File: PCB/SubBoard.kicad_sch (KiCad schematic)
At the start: 37 parts, among them IC1 AS5047P-ATSM, IC2 AS5047P-ATSM, IC3 ICM-20648, J10 Conn_A_Sub, J11 Conn_MCU_L, J4 Conn_ENC_L, J5 SWD, J6 UART, J7 Conn_ENC_R, J8 Conn_MCU_R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

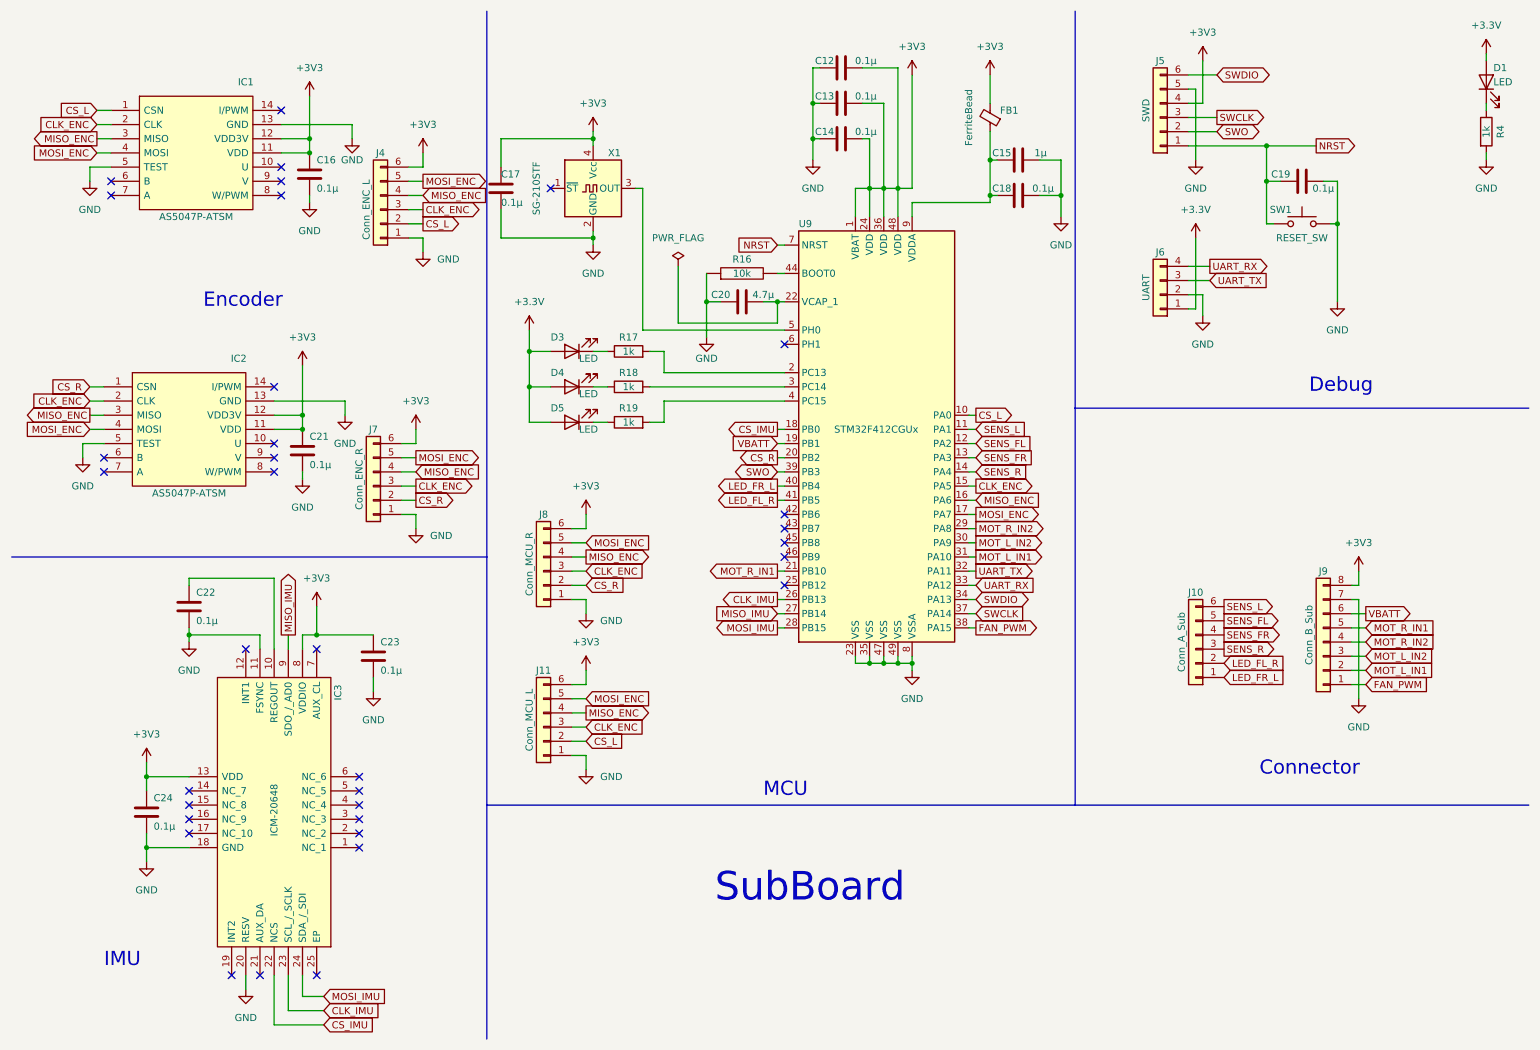
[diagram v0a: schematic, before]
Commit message: [fix]壁センサの配線ミスを修正
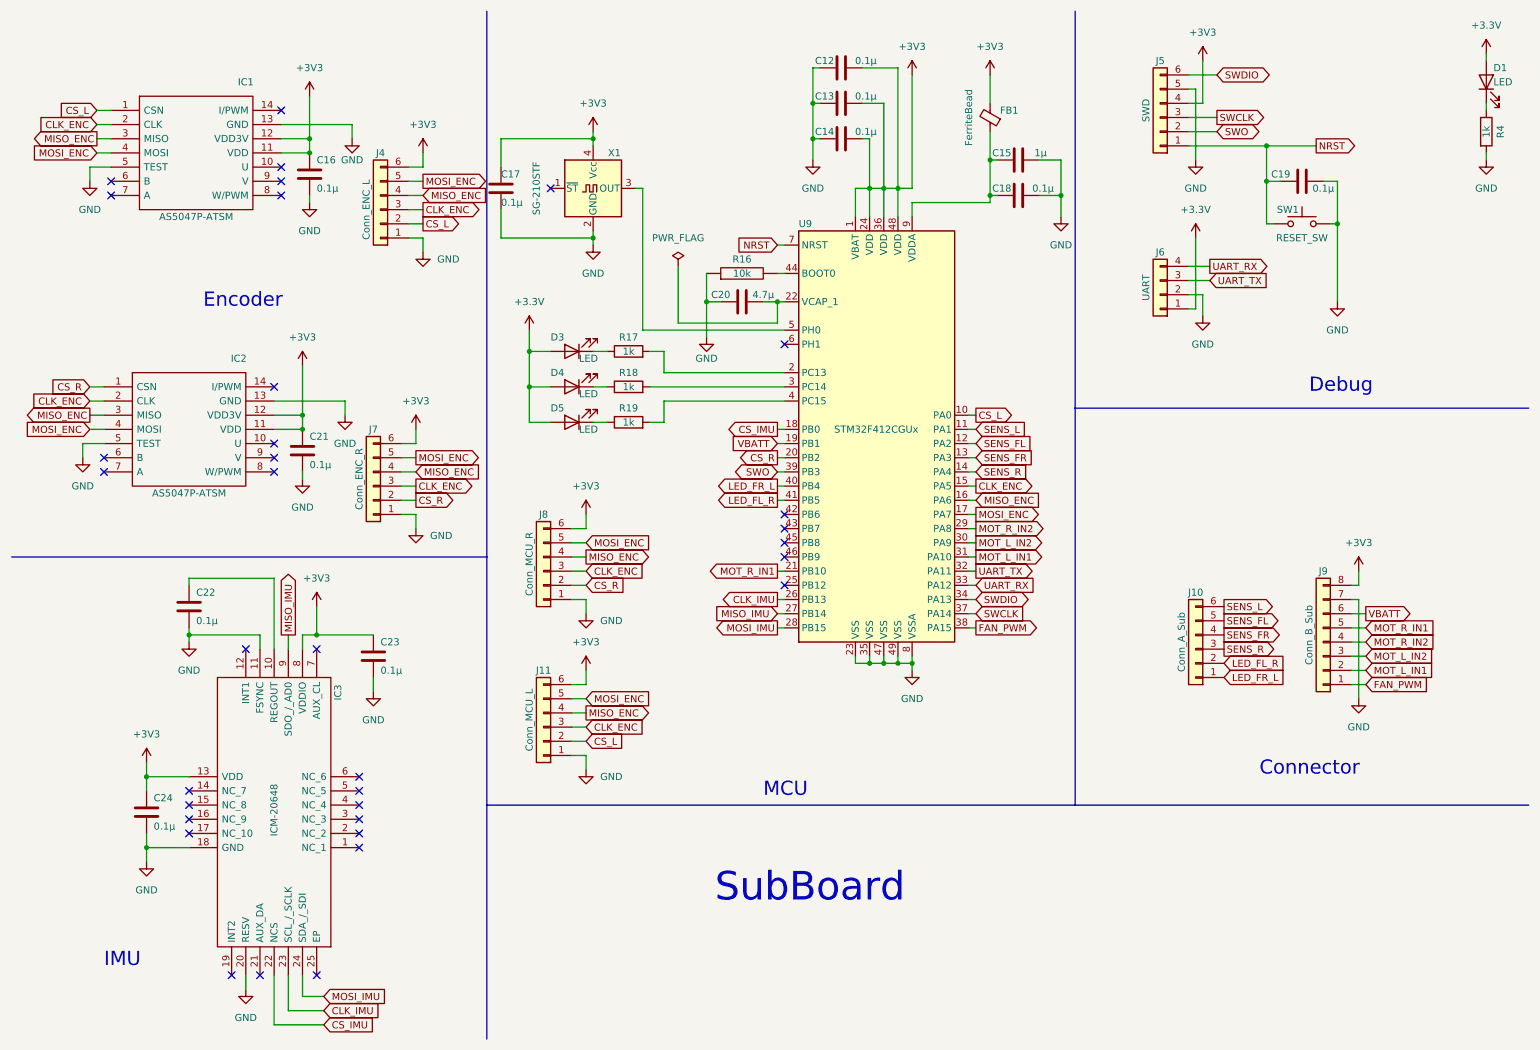
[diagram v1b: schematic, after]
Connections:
- net GND: no longer SW1.2 (A)
- net NRST: now also SW1.2; no longer SW1.3 (B), SW1.4 (B)
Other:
- moved on the sheet: SW1
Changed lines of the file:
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@@
     (pin "4")
   )
-  (symbol (lib_id "Switch:SW_Push") (at 247.65 50.8 270) (mirror x) (unit 1)
+  (symbol (lib_id "Switch:SW_Push") (at 243.84 50.8 0) (mirror y) (unit 1)
     (in_bom yes) (on_board yes)
-    (property "Reference" "SW1" (id 0) (at 240.03 48.26 90))
-    (property "Value" "RESET_SW" (id 1) (at 243.84 53.34 90))
-    (property "Footprint" "SamacSys:SKRPABE010" (id 2) (at 252.73 38.1 0)
+    (property "Reference" "SW1" (id 0) (at 241.3 48.26 0))
+    (property "Value" "RESET_SW" (id 1) (at 243.84 53.34 0))
+    (property "Footprint" "SamacSys:SKRPABE010" (id 2) (at 231.14 45.72 0)
       (effects (font (size 1.27 1.27)) hide)
     )
-    (property "Datasheet" "~" (id 3) (at 247.65 45.72 0)
+    (property "Datasheet" "~" (id 3) (at 238.76 50.8 0)
       (effects (font (size 1.27 1.27)) hide)
     )
     (pin "1")
     (pin "2")
-    (pin "3")
-    (pin "4")
   )
   (symbol (lib_id "power:GND") (at 200.66 49.53 0) (unit 1)
